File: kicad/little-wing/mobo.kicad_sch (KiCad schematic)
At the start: 0 parts

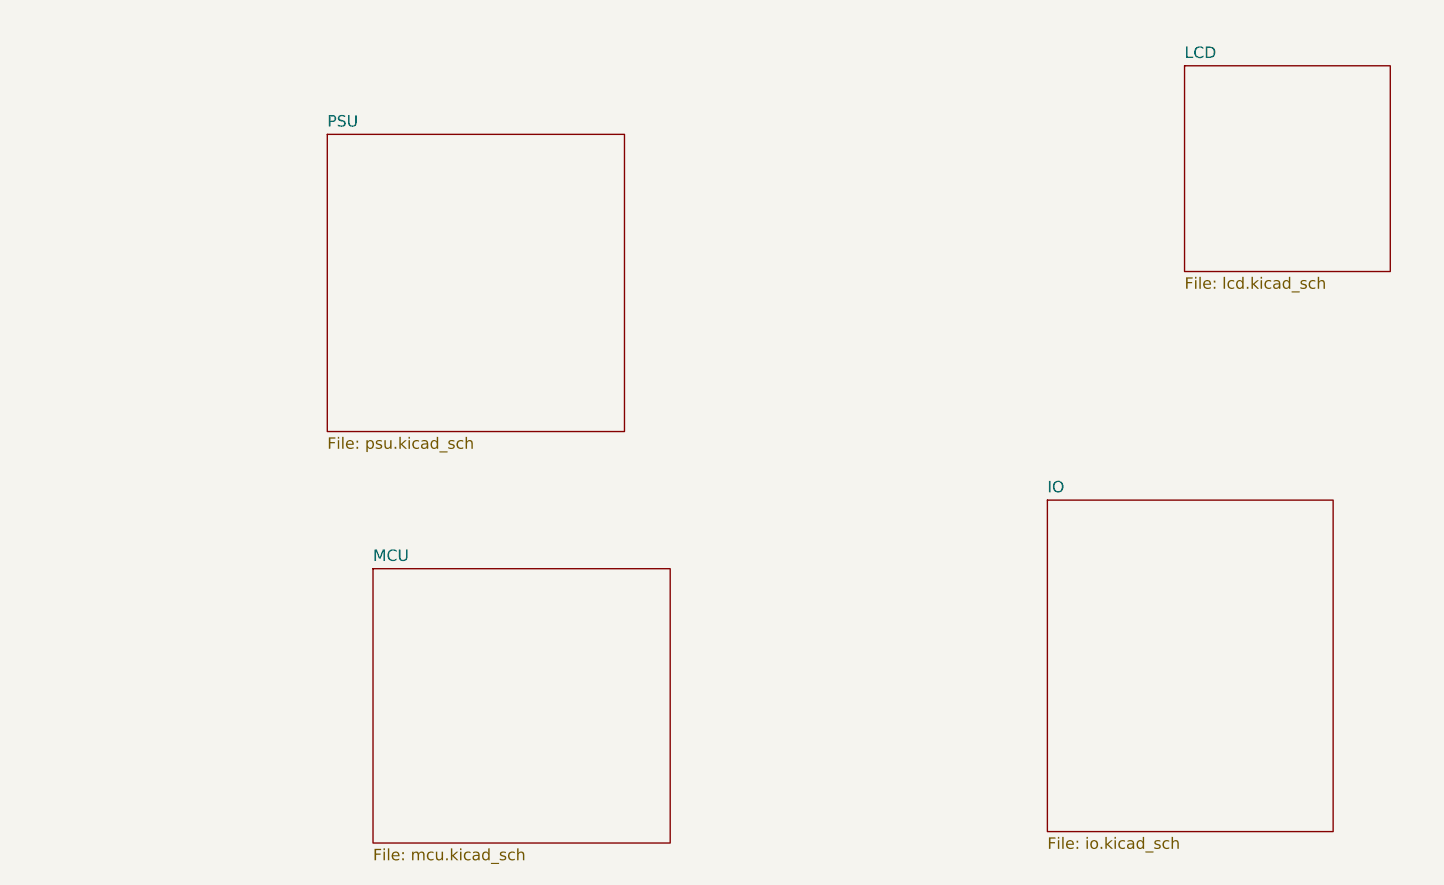
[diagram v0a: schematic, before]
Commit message: Cleaning up the PSU schematics
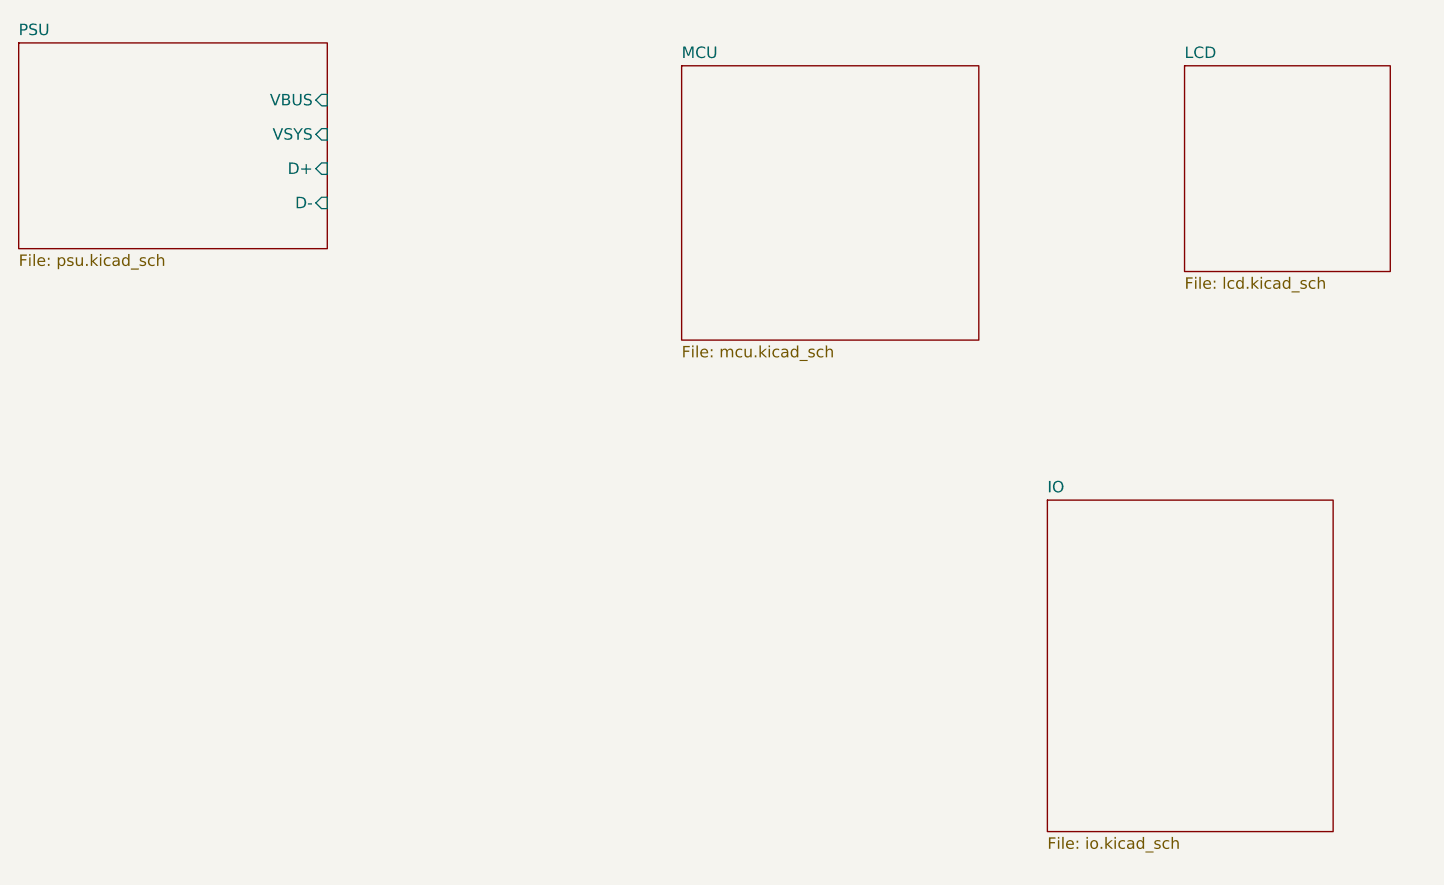
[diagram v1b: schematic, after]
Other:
- sheet PSU ports: added D+, D-, VBUS, VSYS; removed none
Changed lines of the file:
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@@
 	(paper "A4")
 	(sheet
-		(at 104.14 52.07)
-		(size 33.02 33.02)
+		(at 69.85 41.91)
+		(size 34.29 22.86)
 		(exclude_from_sim no)
 		(in_bom yes)
@@
 		)
 		(property "Sheetname" "PSU"
-			(at 104.14 51.3584 0)
+			(at 69.85 41.1984 0)
 			(effects
 				(font
@@
 		)
 		(property "Sheetfile" "psu.kicad_sch"
-			(at 104.14 85.6746 0)
+			(at 69.85 65.3546 0)
 			(effects
 				(font
@@
 				)
 				(justify left top)
+			)
+		)
+		(pin "D+" input
+			(at 104.14 55.88 0)
+			(effects
+				(font
+					(size 1.27 1.27)
+				)
+				(justify right)
+			)
+		)
+		(pin "D-" input
+			(at 104.14 59.69 0)
+			(effects
+				(font
+					(size 1.27 1.27)
+				)
+				(justify right)
+			)
+		)
+		(pin "VBUS" input
+			(at 104.14 48.26 0)
+			(effects
+				(font
+					(size 1.27 1.27)
+				)
+				(justify right)
+			)
+		)
+		(pin "VSYS" input
+			(at 104.14 52.07 0)
+			(effects
+				(font
+					(size 1.27 1.27)
+				)
+				(justify right)
 			)
 		)
@@
 	)
 	(sheet
-		(at 109.22 100.33)
+		(at 143.51 44.45)
 		(size 33.02 30.48)
 		(exclude_from_sim no)
@@
 		)
 		(property "Sheetname" "MCU"
-			(at 109.22 99.6184 0)
+			(at 143.51 43.7384 0)
 			(effects
 				(font
@@
 		)
 		(property "Sheetfile" "mcu.kicad_sch"
-			(at 109.22 131.3946 0)
+			(at 143.51 75.5146 0)
 			(effects
 				(font

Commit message: Cleaning up the schematics a bit more
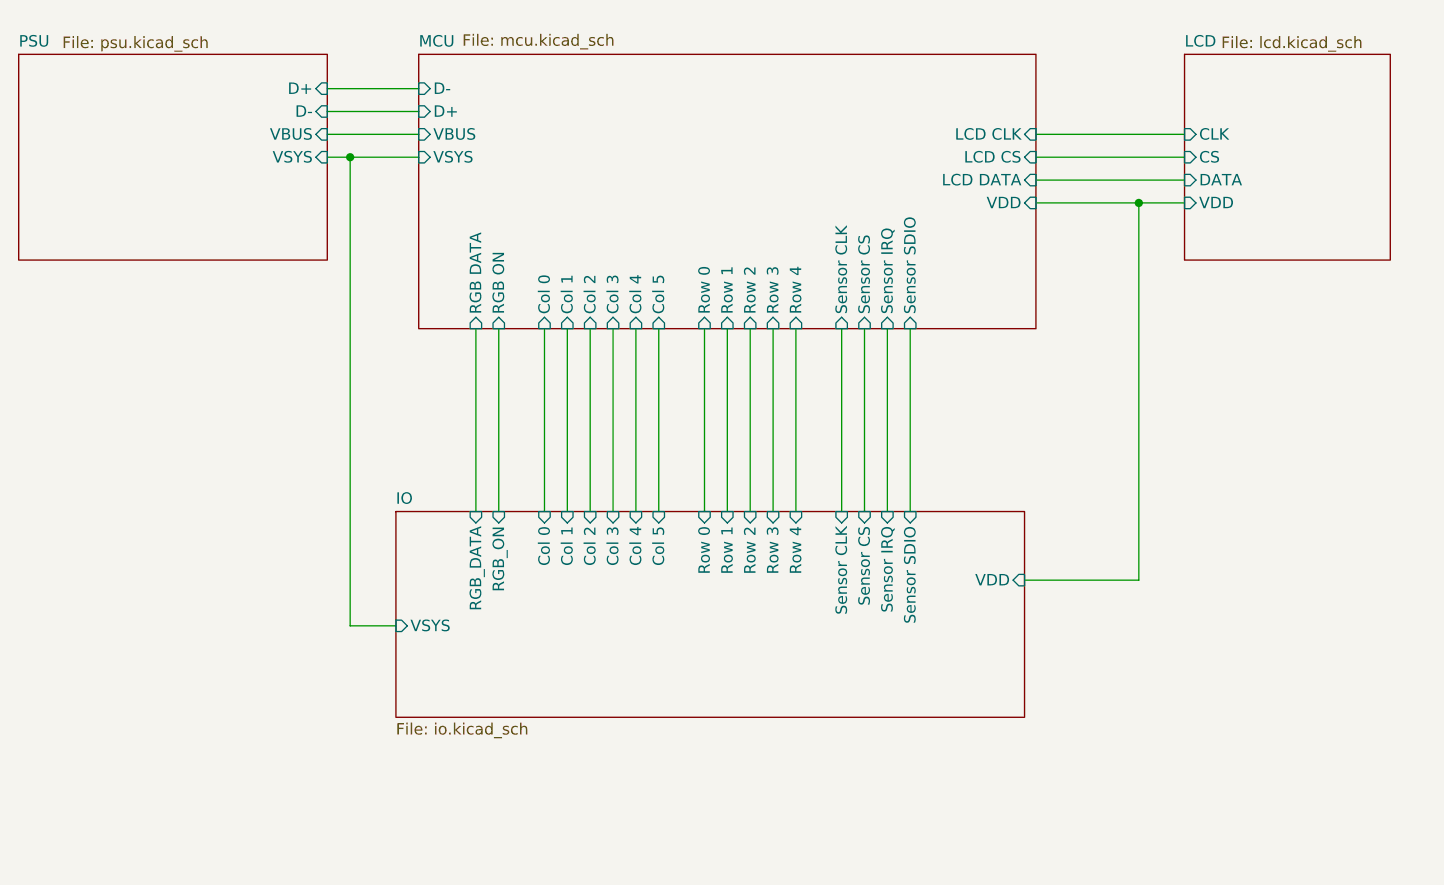
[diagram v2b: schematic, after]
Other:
- sheet IO ports: added Col 0, Col 1, Col 2, Col 3, Col 4, Col 5, RGB_DATA, RGB_ON, Row 0, Row 1, Row 2, Row 3, Row 4, Sensor CLK, Sensor CS, Sensor IRQ, Sensor SDIO, VDD, VSYS; removed none
- sheet LCD ports: added CLK, CS, DATA, VDD; removed none
- sheet MCU ports: added Col 0, Col 1, Col 2, Col 3, Col 4, Col 5, D+, D-, LCD CLK, LCD CS, LCD DATA, RGB DATA, RGB ON, Row 0, Row 1, Row 2, Row 3, Row 4, Sensor CLK, Sensor CS, Sensor IRQ, Sensor SDIO, VBUS, VDD, VSYS; removed none

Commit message: Reseting all the extra components sizes
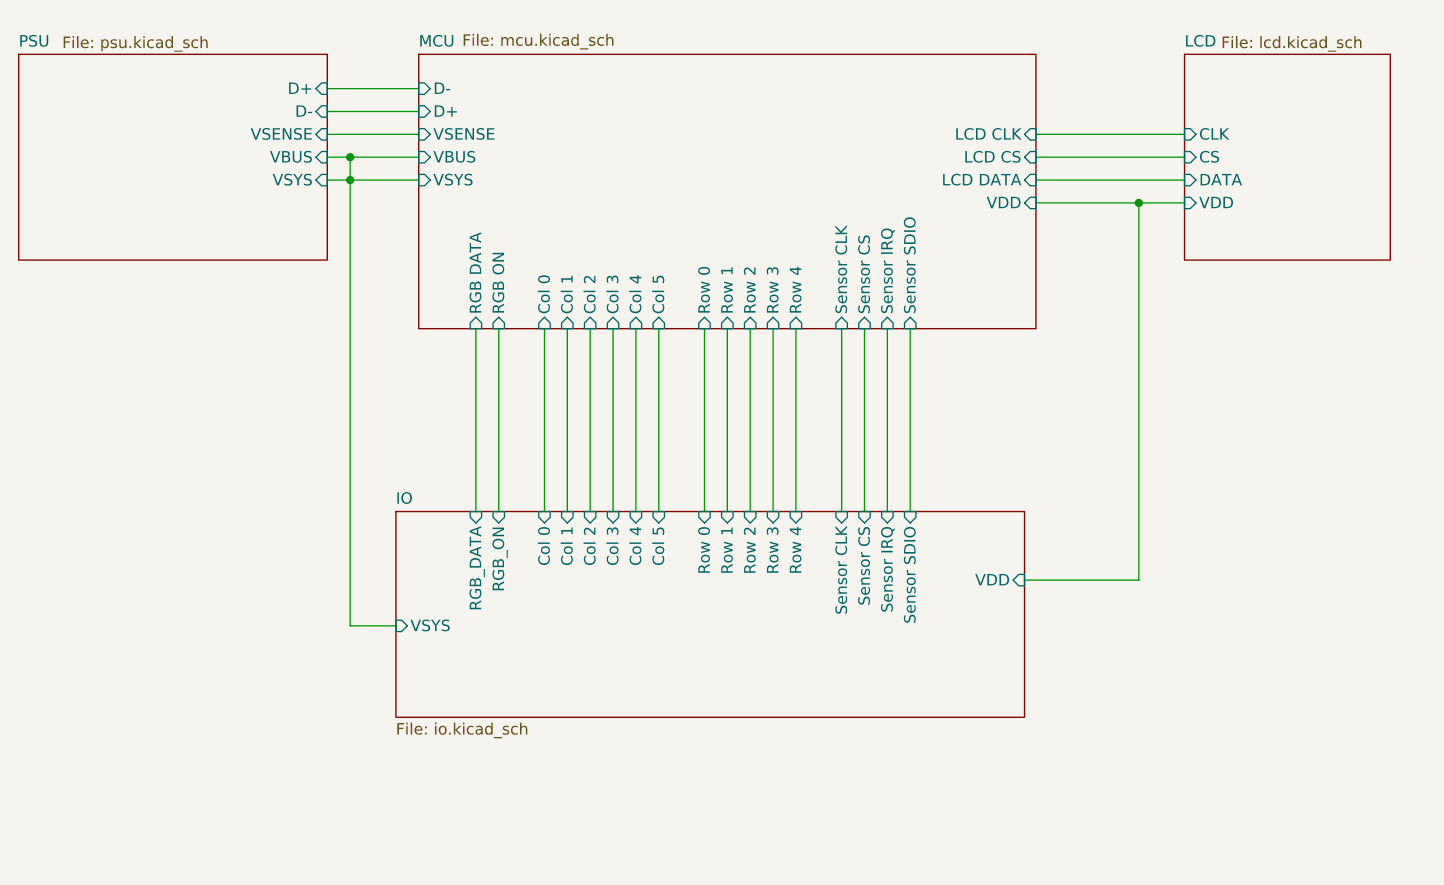
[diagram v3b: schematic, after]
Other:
- sheet MCU ports: added VSENSE; removed none
- sheet PSU ports: added VSENSE; removed none
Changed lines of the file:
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@@
 		(color 0 0 0 0)
 	)
+	(junction
+		(at 106.68 57.15)
+		(diameter 0)
+		(color 0 0 0 0)
+	)
+	(wire
+		(pts
+			(xy 104.14 57.15) (xy 106.68 57.15)
+		)
+		(stroke
+			(width 0)
+			(type default)
+		)
+	)
+	(wire
+		(pts
+			(xy 182.88 54.61) (xy 199.39 54.61)
+		)
+		(stroke
+			(width 0)
+			(type default)
+		)
+	)
+	(wire
+		(pts
+			(xy 123.19 73.66) (xy 123.19 93.98)
+		)
+		(stroke
+			(width 0)
+			(type default)
+		)
+	)
+	(wire
+		(pts
+			(xy 182.88 57.15) (xy 199.39 57.15)
+		)
+		(stroke
+			(width 0)
+			(type default)
+		)
+	)
+	(wire
+		(pts
+			(xy 153.67 73.66) (xy 153.67 93.98)
+		)
+		(stroke
+			(width 0)
+			(type default)
+		)
+	)
+	(wire
+		(pts
+			(xy 148.59 73.66) (xy 148.59 93.98)
+		)
+		(stroke
+			(width 0)
+			(type default)
+		)
+	)
+	(wire
+		(pts
+			(xy 194.31 59.69) (xy 199.39 59.69)
+		)
+		(stroke
+			(width 0)
+			(type default)
+		)
+	)
+	(wire
+		(pts
+			(xy 106.68 106.68) (xy 111.76 106.68)
+		)
+		(stroke
+			(width 0)
+			(type default)
+		)
+	)
+	(wire
+		(pts
+			(xy 163.83 73.66) (xy 163.83 93.98)
+		)
+		(stroke
+			(width 0)
+			(type default)
+		)
+	)
+	(wire
+		(pts
+			(xy 181.61 101.6) (xy 194.31 101.6)
+		)
+		(stroke
+			(width 0)
+			(type default)
+		)
+	)
+	(wire
+		(pts
+			(xy 161.29 73.66) (xy 161.29 93.98)
+		)
+		(stroke
+			(width 0)
+			(type default)
+		)
+	)
+	(wire
+		(pts
+			(xy 106.68 57.15) (xy 106.68 106.68)
+		)
+		(stroke
+			(width 0)
+			(type default)
+		)
+	)
+	(wire
+		(pts
+			(xy 106.68 57.15) (xy 106.68 54.61)
+		)
+		(stroke
+			(width 0)
+			(type default)
+		)
+	)
+	(wire
+		(pts
+			(xy 104.14 52.07) (xy 114.3 52.07)
+		)
+		(stroke
+			(width 0)
+			(type default)
+		)
+	)
 	(wire
 		(pts
@@
 	(wire
 		(pts
-			(xy 182.88 54.61) (xy 199.39 54.61)
-		)
-		(stroke
-			(width 0)
-			(type default)
-		)
-	)
-	(wire
-		(pts
-			(xy 123.19 73.66) (xy 123.19 93.98)
-		)
-		(stroke
-			(width 0)
-			(type default)
-		)
-	)
-	(wire
-		(pts
-			(xy 182.88 57.15) (xy 199.39 57.15)
-		)
-		(stroke
-			(width 0)
-			(type default)
-		)
-	)
-	(wire
-		(pts
-			(xy 153.67 73.66) (xy 153.67 93.98)
-		)
-		(stroke
-			(width 0)
-			(type default)
-		)
-	)
-	(wire
-		(pts
-			(xy 148.59 73.66) (xy 148.59 93.98)
-		)
-		(stroke
-			(width 0)
-			(type default)
-		)
-	)
-	(wire
-		(pts
-			(xy 194.31 59.69) (xy 199.39 59.69)
-		)
-		(stroke
-			(width 0)
-			(type default)
-		)
-	)
-	(wire
-		(pts
-			(xy 106.68 106.68) (xy 111.76 106.68)
-		)
-		(stroke
-			(width 0)
-			(type default)
-		)
-	)
-	(wire
-		(pts
-			(xy 163.83 73.66) (xy 163.83 93.98)
-		)
-		(stroke
-			(width 0)
-			(type default)
-		)
-	)
-	(wire
-		(pts
-			(xy 106.68 54.61) (xy 106.68 106.68)
-		)
-		(stroke
-			(width 0)
-			(type default)
-		)
-	)
-	(wire
-		(pts
-			(xy 181.61 101.6) (xy 194.31 101.6)
-		)
-		(stroke
-			(width 0)
-			(type default)
-		)
-	)
-	(wire
-		(pts
-			(xy 161.29 73.66) (xy 161.29 93.98)
-		)
-		(stroke
-			(width 0)
-			(type default)
-		)
-	)
-	(wire
-		(pts
-			(xy 104.14 52.07) (xy 114.3 52.07)
+			(xy 106.68 57.15) (xy 114.3 57.15)
+		)
+		(stroke
+			(width 0)
+			(type default)
+		)
+	)
+	(wire
+		(pts
+			(xy 128.27 73.66) (xy 128.27 93.98)
+		)
+		(stroke
+			(width 0)
+			(type default)
+		)
+	)
+	(wire
+		(pts
+			(xy 168.91 73.66) (xy 168.91 93.98)
+		)
+		(stroke
+			(width 0)
+			(type default)
+		)
+	)
+	(wire
+		(pts
+			(xy 194.31 101.6) (xy 194.31 59.69)
+		)
+		(stroke
+			(width 0)
+			(type default)
+		)
+	)
+	(wire
+		(pts
+			(xy 151.13 73.66) (xy 151.13 93.98)
+		)
+		(stroke
+			(width 0)
+			(type default)
+		)
+	)
+	(wire
+		(pts
+			(xy 104.14 46.99) (xy 114.3 46.99)
+		)
+		(stroke
+			(width 0)
+			(type default)
+		)
+	)
+	(wire
+		(pts
+			(xy 156.21 73.66) (xy 156.21 93.98)
+		)
+		(stroke
+			(width 0)
+			(type default)
+		)
+	)
+	(wire
+		(pts
+			(xy 104.14 49.53) (xy 114.3 49.53)
 		)
 		(stroke
@@
 		(pts
 			(xy 106.68 54.61) (xy 114.3 54.61)
-		)
-		(stroke
-			(width 0)
-			(type default)
-		)
-	)
-	(wire
-		(pts
-			(xy 128.27 73.66) (xy 128.27 93.98)
-		)
-		(stroke
-			(width 0)
-			(type default)
-		)
-	)
-	(wire
-		(pts
-			(xy 168.91 73.66) (xy 168.91 93.98)
-		)
-		(stroke
-			(width 0)
-			(type default)
-		)
-	)
-	(wire
-		(pts
-			(xy 194.31 101.6) (xy 194.31 59.69)
-		)
-		(stroke
-			(width 0)
-			(type default)
-		)
-	)
-	(wire
-		(pts
-			(xy 151.13 73.66) (xy 151.13 93.98)
-		)
-		(stroke
-			(width 0)
-			(type default)
-		)
-	)
-	(wire
-		(pts
-			(xy 104.14 46.99) (xy 114.3 46.99)
-		)
-		(stroke
-			(width 0)
-			(type default)
-		)
-	)
-	(wire
-		(pts
-			(xy 156.21 73.66) (xy 156.21 93.98)
-		)
-		(stroke
-			(width 0)
-			(type default)
-		)
-	)
-	(wire
-		(pts
-			(xy 104.14 49.53) (xy 114.3 49.53)
 		)
 		(stroke
@@
 		)
 		(pin "VBUS" input
+			(at 104.14 54.61 0)
+			(effects
+				(font
+					(size 1.27 1.27)
+				)
+				(justify right)
+			)
+		)
+		(pin "VSYS" input
+			(at 104.14 57.15 0)
+			(effects
+				(font
+					(size 1.27 1.27)
+				)
+				(justify right)
+			)
+		)
+		(pin "VSENSE" input
 			(at 104.14 52.07 0)
-			(effects
-				(font
-					(size 1.27 1.27)
-				)
-				(justify right)
-			)
-		)
-		(pin "VSYS" input
-			(at 104.14 54.61 0)
 			(effects
 				(font
@@
 		)
 		(pin "VBUS" input
-			(at 114.3 52.07 180)
+			(at 114.3 54.61 180)
 			(effects
 				(font
@@
 		)
 		(pin "VSYS" input
-			(at 114.3 54.61 180)
+			(at 114.3 57.15 180)
 			(effects
 				(font
@@
 			(effects
 				(font
+					(size 1.27 1.27)
+				)
+				(justify left)
+			)
+		)
+		(pin "VSENSE" input
+			(at 114.3 52.07 180)
+			(effects
+				(font

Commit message: Fixes and space optimisations
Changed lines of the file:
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@@
 	(paper "A4")
-	(junction
-		(at 106.68 54.61)
-		(diameter 0)
-		(color 0 0 0 0)
-	)
 	(junction
 		(at 194.31 59.69)
@@
 	(wire
 		(pts
-			(xy 106.68 57.15) (xy 106.68 54.61)
-		)
-		(stroke
-			(width 0)
-			(type default)
-		)
-	)
-	(wire
-		(pts
 			(xy 104.14 52.07) (xy 114.3 52.07)
 		)
@@
 	(wire
 		(pts
-			(xy 104.14 54.61) (xy 106.68 54.61)
+			(xy 104.14 54.61) (xy 114.3 54.61)
 		)
 		(stroke
@@
 		)
 		(stroke
-			(width 0)
-			(type default)
-		)
-	)
-	(wire
-		(pts
-			(xy 106.68 54.61) (xy 114.3 54.61)
-		)
-		(stroke

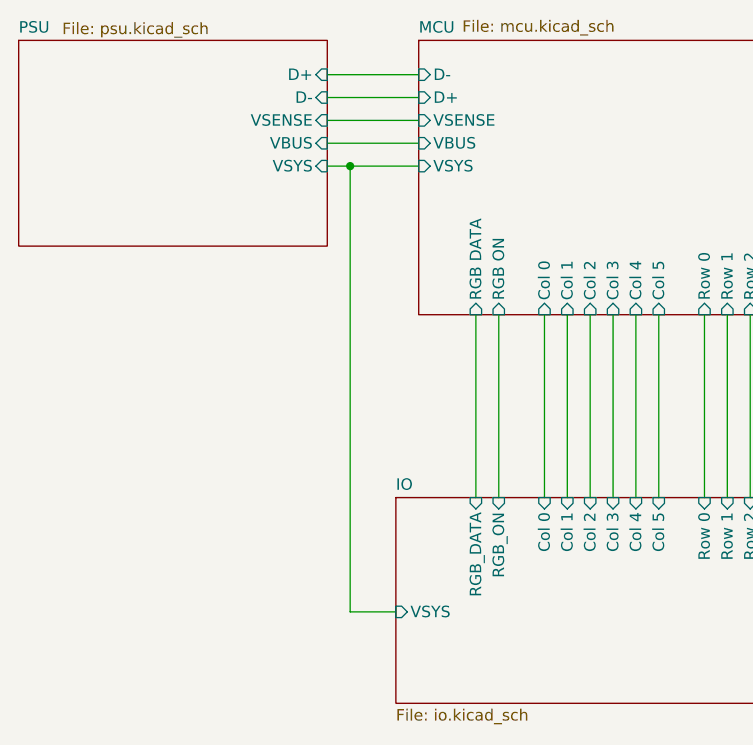
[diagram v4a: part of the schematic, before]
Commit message: Connecting remaining power lines
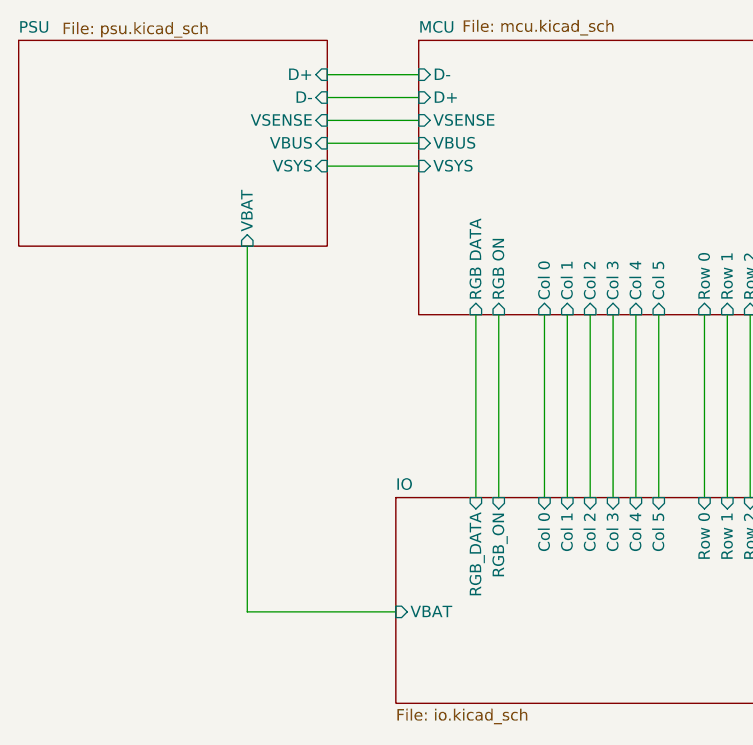
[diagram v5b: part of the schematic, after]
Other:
- sheet IO ports: added VBAT; removed VSYS
- sheet PSU ports: added VBAT; removed none
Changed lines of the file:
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@@
 		(color 0 0 0 0)
 	)
-	(junction
-		(at 106.68 57.15)
-		(diameter 0)
-		(color 0 0 0 0)
-	)
-	(wire
-		(pts
-			(xy 104.14 57.15) (xy 106.68 57.15)
-		)
-		(stroke
-			(width 0)
-			(type default)
-		)
-	)
 	(wire
 		(pts
@@
 	(wire
 		(pts
-			(xy 106.68 106.68) (xy 111.76 106.68)
-		)
-		(stroke
-			(width 0)
-			(type default)
-		)
-	)
-	(wire
-		(pts
 			(xy 163.83 73.66) (xy 163.83 93.98)
 		)
@@
 	(wire
 		(pts
-			(xy 106.68 57.15) (xy 106.68 106.68)
-		)
-		(stroke
-			(width 0)
-			(type default)
-		)
-	)
-	(wire
-		(pts
 			(xy 104.14 52.07) (xy 114.3 52.07)
 		)
@@
 	(wire
 		(pts
-			(xy 106.68 57.15) (xy 114.3 57.15)
+			(xy 95.25 66.04) (xy 95.25 106.68)
+		)
+		(stroke
+			(width 0)
+			(type default)
+		)
+	)
+	(wire
+		(pts
+			(xy 104.14 57.15) (xy 114.3 57.15)
 		)
 		(stroke
@@
 		(pts
 			(xy 182.88 52.07) (xy 199.39 52.07)
+		)
+		(stroke
+			(width 0)
+			(type default)
+		)
+	)
+	(wire
+		(pts
+			(xy 95.25 106.68) (xy 111.76 106.68)
 		)
 		(stroke
@@
 				)
 				(justify right)
+			)
+		)
+		(pin "VBAT" input
+			(at 95.25 66.04 270)
+			(effects
+				(font
+					(size 1.27 1.27)
+				)
+				(justify left)
 			)
 		)
@@
 			)
 		)
-		(pin "VSYS" input
+		(pin "VBAT" input
 			(at 111.76 106.68 180)
 			(effects
